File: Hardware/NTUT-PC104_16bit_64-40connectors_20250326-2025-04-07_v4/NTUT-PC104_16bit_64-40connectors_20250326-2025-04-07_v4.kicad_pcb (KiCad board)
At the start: 4 copper layers, 390.3 x 285.7 mm, 43 parts, among them J10 Conn_02x26_Odd_Even, J12 Conn_02x04_Odd_Even, J13 Conn_02x04_Odd_Even, J14 Conn_02x04_Odd_Even, J15 Conn_02x04_Odd_Even, J16 Conn_02x04_Odd_Even, J17 Conn_02x04_Odd_Even, J18 Conn_02x04_Odd_Even, J7 Conn_02x04_Odd_Even, J8 Conn_02x26_Odd_Even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

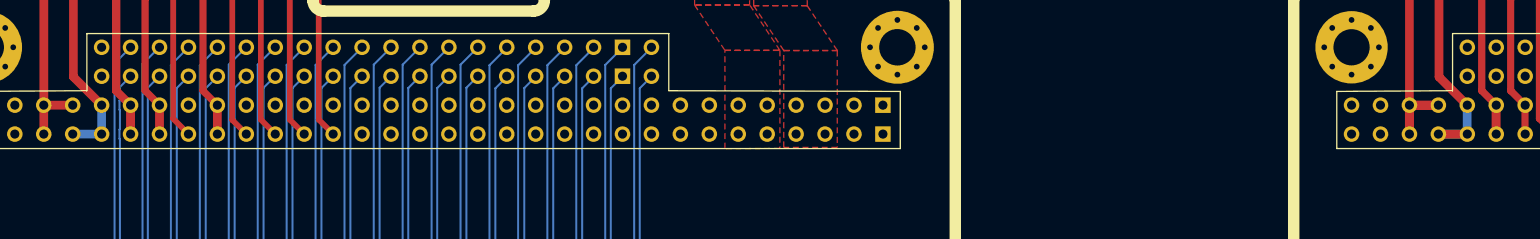
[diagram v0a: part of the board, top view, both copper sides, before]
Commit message: Module 2 Module 4 dc_bus_1 repaint
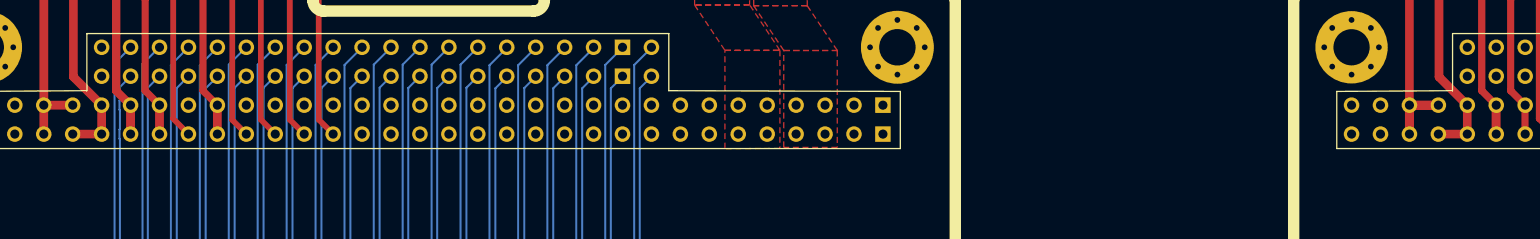
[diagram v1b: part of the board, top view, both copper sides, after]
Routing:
- net /DC_BUS_1: track 802.6 -> 800.1 mm
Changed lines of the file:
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@@
 			(keep_text_aligned yes)
 		)
-		(gr_text "4722.9213 mils"
+		(gr_text "119.9622 mm"
 			(at 90.6897 337.5212 0)
 			(layer "Eco1.User")
@@
 	)
 	(segment
+		(start 60.19 228.495)
+		(end 57.65 228.495)
+		(width 0.762)
+		(layer "F.Cu")
+		(net 63)
+	)
+	(segment
 		(start 177.5798 223.4742)
 		(end 180.0606 225.955)
@@
 	)
 	(segment
+		(start 60.19 225.955)
+		(end 60.19 228.495)
+		(width 0.762)
+		(layer "F.Cu")
+		(net 63)
+	)
+	(segment
 		(start 297.1354 107.27)
 		(end 297.1608 107.2954)
@@
 	)
 	(segment
+		(start 180.065 225.955)
+		(end 180.065 228.495)
+		(width 0.762)
+		(layer "F.Cu")
+		(net 63)
+	)
+	(segment
 		(start 177.525 228.495)
 		(end 180.065 228.495)
@@
 	)
 	(segment
-		(start 57.65 228.495)
-		(end 60.19 228.495)
-		(width 0.762)
-		(layer "B.Cu")
-		(net 63)
-	)
-	(segment
-		(start 180.0526 225.955)
-		(end 180.0526 228.495)
-		(width 0.762)
-		(layer "B.Cu")
-		(net 63)
-	)
-	(segment
-		(start 177.5126 228.495)
-		(end 180.0526 228.495)
-		(width 0.762)
-		(layer "B.Cu")
-		(net 63)
-	)
-	(segment
 		(start 30.226 113.5278)
 		(end 57.6326 113.5278)
 		(width 0.762)
 		(layer "B.Cu")
-		(net 63)
-	)
-	(segment
-		(start 60.19 225.955)
-		(end 60.19 228.495)
-		(width 0.762)
-		(layer "B.Cu")
